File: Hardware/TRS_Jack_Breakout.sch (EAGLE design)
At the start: 7 parts

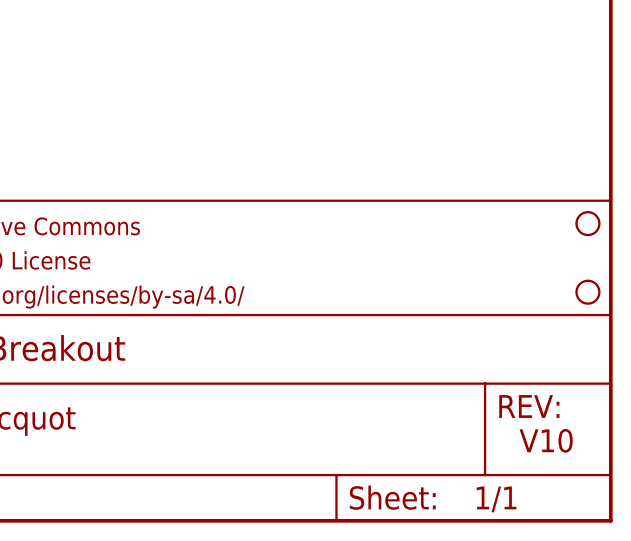
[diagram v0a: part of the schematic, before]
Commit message: Updates after red review.
Wider outline on dimension layer, added gear logo.
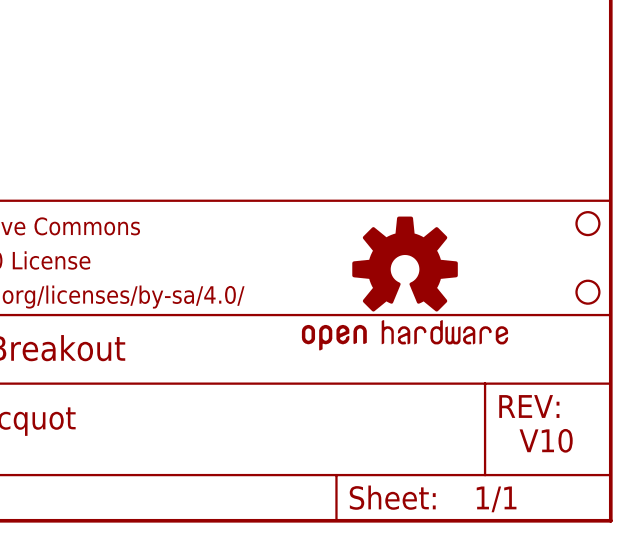
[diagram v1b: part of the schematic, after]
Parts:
- added LOGO2: OSHW-LOGOS, SparkFun-Aesthetics:OSHW-LOGOS
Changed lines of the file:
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@@
 <part name="STANDOFF2" library="SparkFun-Electromechanical" deviceset="STAND-OFF" device=""/>
 <part name="JP2" library="SparkFun-Connectors" deviceset="M01" device="SMDNS"/>
+<part name="LOGO2" library="SparkFun-Aesthetics" deviceset="OSHW-LOGO" device="S"/>
 </parts>
 <sheets>
@@
 <instance part="STANDOFF2" gate="G$1" x="246.38" y="25.4"/>
 <instance part="JP2" gate="G$1" x="104.14" y="93.98"/>
+<instance part="LOGO2" gate="G$1" x="226.06" y="27.94"/>
 </instances>
 <busses>
